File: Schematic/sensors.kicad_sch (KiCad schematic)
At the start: 17 parts, among them IC4 ICM-42688-P, IC5 MPU-6500, U5 SPL06-001, U7 QMC5883L

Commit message: schematic fully finished, every footprint assigned, still electrical checking to do
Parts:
- IC4: footprint IIM42352 -> fch7_fp:LGA-16_L3.0-W3.0-P0.50-BL_SQ
- IC5: footprint QFN40P300X300X95-25M-D -> fch7_fp:QFN40P300X300X95-25M-D
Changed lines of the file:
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@@
 			)
 		)
-		(property "Footprint" "IIM42352"
+		(property "Footprint" "fch7_fp:LGA-16_L3.0-W3.0-P0.50-BL_SQ"
 			(at 256.54 131.75 0)
 			(effects
@@
 			)
 		)
-		(property "Footprint" "QFN40P300X300X95-25M-D"
+		(property "Footprint" "fch7_fp:QFN40P300X300X95-25M-D"
 			(at 140.97 143.18 0)
 			(effects

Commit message: reviewing and refactoring footprints and full schematic
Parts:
- C28, C29, C30, C31, C32, C33, C34, C36: MPN (none) -> 0603B104K500NT; Manufacturer (none) -> FH
- C35, C37: MPN (none) -> CC0603KRX7R9BB103; Manufacturer (none) -> YAGEO
- C38: MPN (none) -> 0603B224K500NT; Manufacturer (none) -> FH
- C39: footprint Capacitor_SMD:C_0805_2012Metric -> Capacitor_SMD:C_0603_1608Metric; MPN (none) -> CL10B105KO8NNNC; Manufacturer (none) -> SAMSUNG
- IC4: MPN (none) -> ICM-42688-P; Manufacturer (none) -> TDK
- IC5: MPN (none) -> MPU-6500; Manufacturer (none) -> TDK
- R22: MPN (none) -> RC0603FR-07100KL; Manufacturer (none) -> YAGEO
- U5: MPN (none) -> SPL06-001; Manufacturer (none) -> Goertek
- U7: MPN (none) -> QMC5883L; Manufacturer (none) -> QST

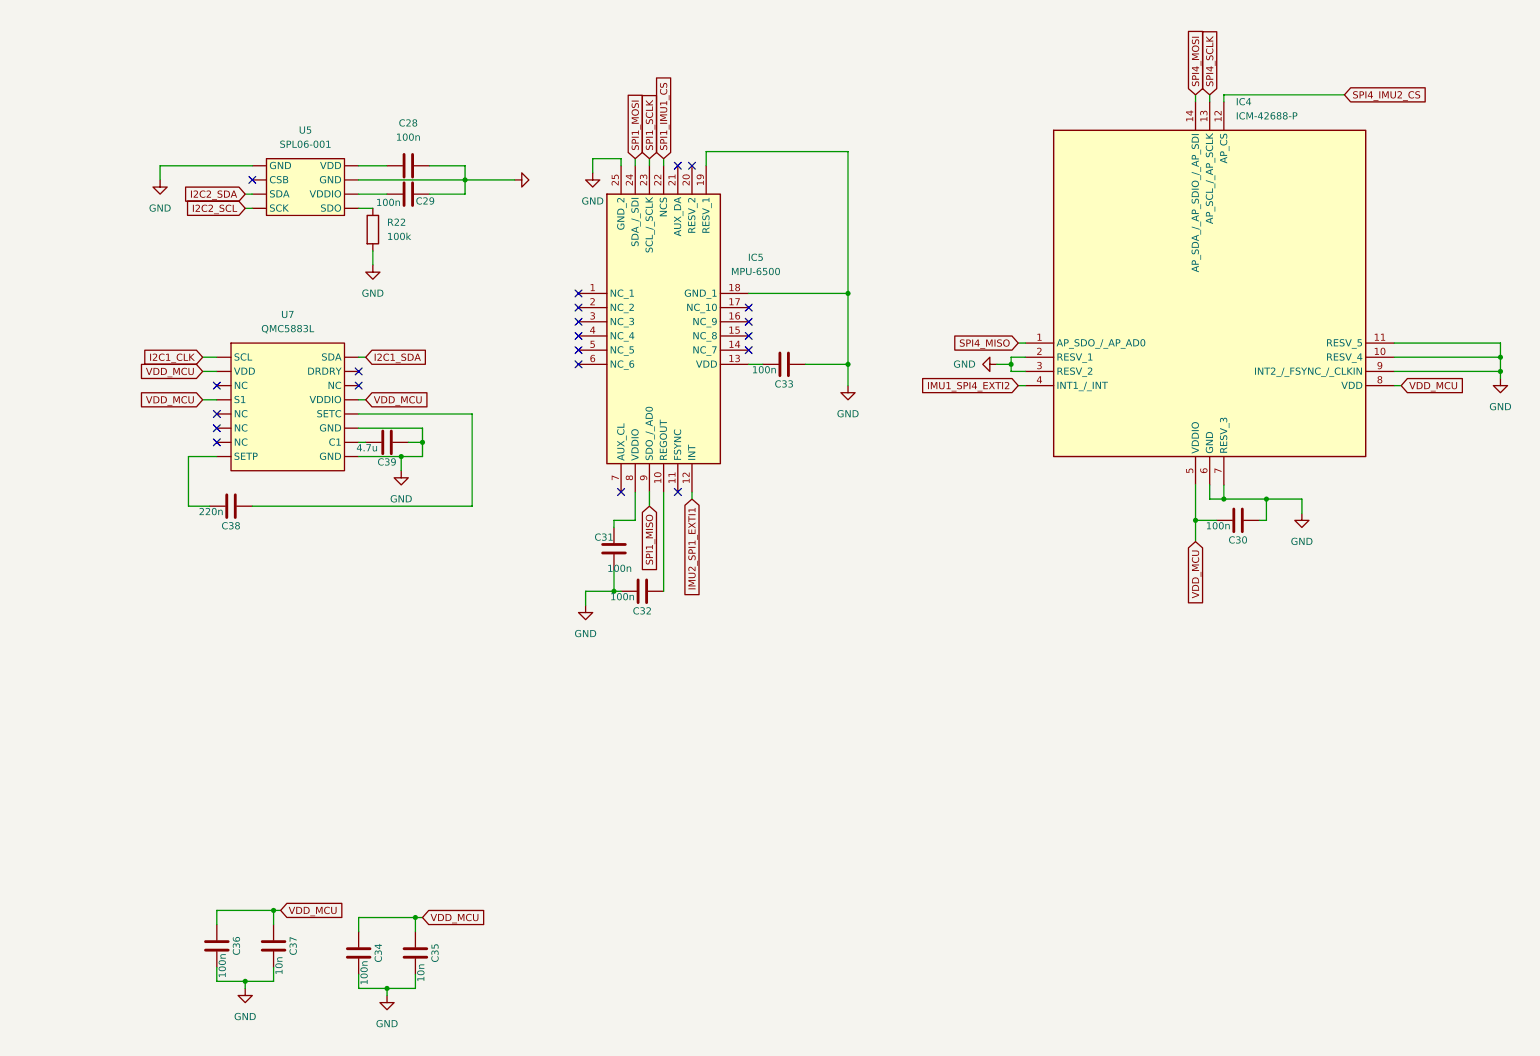
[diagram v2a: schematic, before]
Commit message: Update schematic and footprint libraries with various component modifications
- Updated fp-info-cache with new component details and footprint changes.
- Modified osd.kicad_sch to correct pin types and add no_connect entries.
- Adjusted rf_rx.kicad_sch to fix pin assignments and update component properties.
- Enhanced sensors.kicad_sch with new properties for QMC5883L and SPL06-001 sensors.
- Added new libraries to sym-lib-table and fp-lib-table for better organization and access to components.
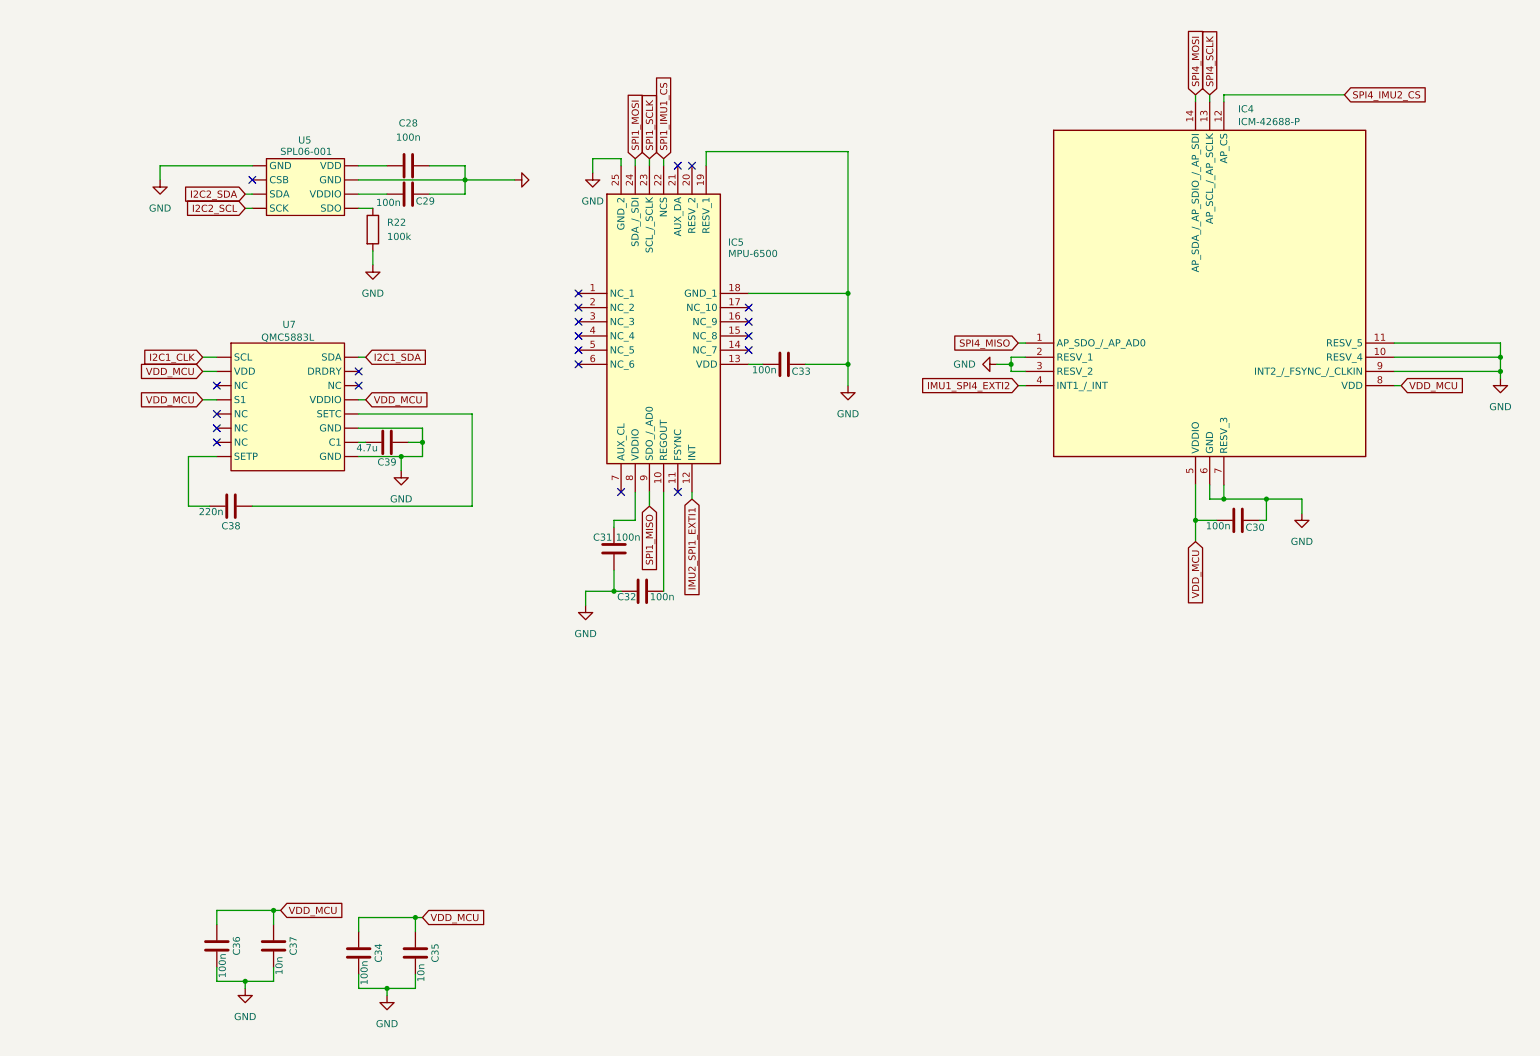
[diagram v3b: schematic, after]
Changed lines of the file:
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@@
 		(dnp no)
 		(property "Reference" "C32"
-			(at 125.73 120.396 90)
+			(at 122.936 117.856 90)
 			(effects
 				(font
@@
 		)
 		(property "Value" "100n"
-			(at 122.174 117.856 90)
+			(at 129.286 117.856 90)
 			(effects
 				(font
@@
 		(on_board yes)
 		(dnp no)
-		(fields_autoplaced yes)
 		(property "Reference" "U7"
-			(at 62.23 67.31 0)
+			(at 62.484 69.088 0)
 			(effects
 				(font
@@
 		)
 		(property "Value" "QMC5883L"
-			(at 62.23 69.85 0)
+			(at 62.23 71.374 0)
 			(effects
 				(font
@@
 		(dnp no)
 		(property "Reference" "C31"
-			(at 118.872 107.188 0)
+			(at 118.618 107.188 0)
 			(effects
 				(font
@@
 		)
 		(property "Value" "100n"
-			(at 121.666 112.776 0)
+			(at 123.19 107.188 0)
 			(effects
 				(font
@@
 		(dnp no)
 		(property "Reference" "C33"
-			(at 151.13 79.756 90)
+			(at 154.178 77.47 90)
 			(effects
 				(font
@@
 		(on_board yes)
 		(dnp no)
-		(fields_autoplaced yes)
 		(property "Reference" "IC4"
-			(at 232.0133 29.21 0)
+			(at 232.41 30.48 0)
 			(effects
 				(font
@@
 		)
 		(property "Value" "ICM-42688-P"
-			(at 232.0133 31.75 0)
+			(at 232.41 32.766 0)
 			(effects
 				(font
@@
 		(dnp no)
 		(property "Reference" "C30"
-			(at 232.41 107.696 90)
+			(at 235.458 105.41 90)
 			(effects
 				(font
@@
 		(on_board yes)
 		(dnp no)
-		(fields_autoplaced yes)
 		(property "Reference" "U5"
-			(at 65.405 34.29 0)
+			(at 65.278 36.068 0)
 			(effects
 				(font
@@
 		)
 		(property "Value" "SPL06-001"
-			(at 65.405 36.83 0)
+			(at 65.532 38.1 0)
 			(effects
 				(font
@@
 		(on_board yes)
 		(dnp no)
-		(fields_autoplaced yes)
 		(property "Reference" "IC5"
-			(at 146.05 57.0798 0)
+			(at 142.494 54.356 0)
 			(effects
 				(font
@@
 		)
 		(property "Value" "MPU-6500"
-			(at 146.05 59.6198 0)
-			(effects
-				(font
+			(at 145.542 56.388 0)
+			(effects
+				(font

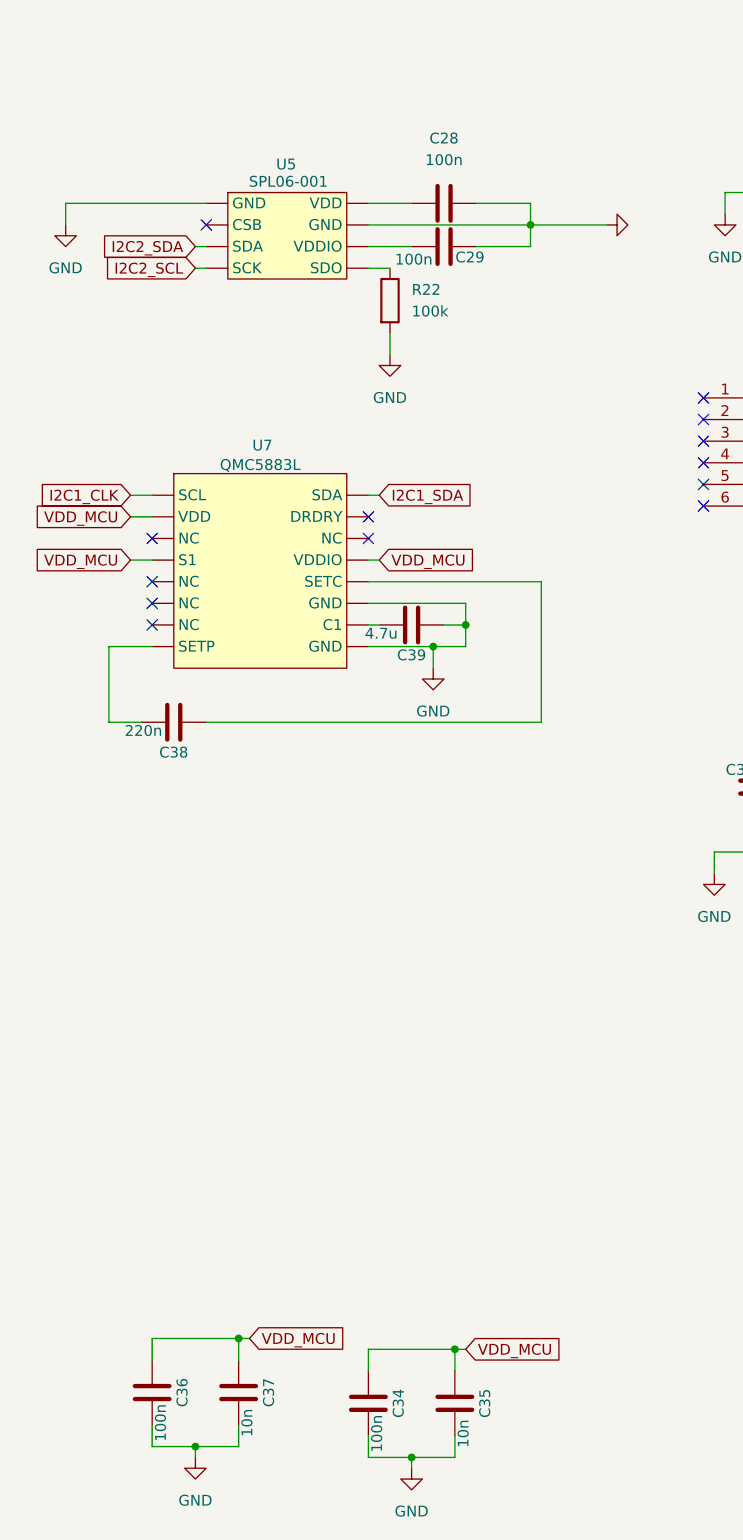
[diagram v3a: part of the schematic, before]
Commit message: Refactor fp-lib-table: Remove unused libraries and update description for fch7_fp
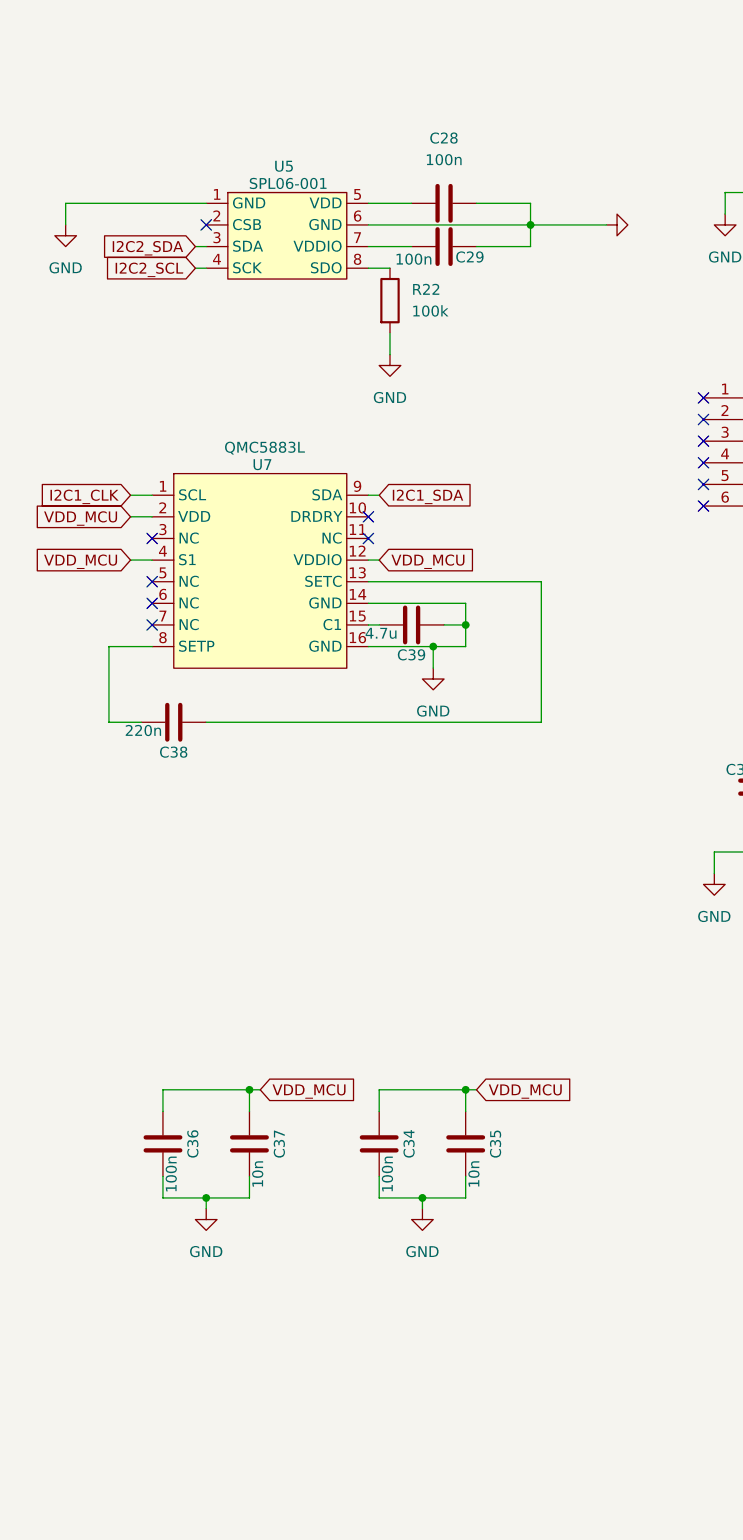
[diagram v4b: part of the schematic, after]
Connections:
- net GND: now also U5.1 (GND), U5.6 (GND), U7.14 (GND), U7.16 (GND); no longer U5. (SDO), U7. (GND)
- net I2C1_CLK: now also U7.1 (SCL); no longer U7. (GND)
- net I2C1_SDA: now also U7.9 (SDA); no longer U7. (GND)
- net I2C2_SCL: now also U5.4 (SCK); no longer U5. (SDO)
- net I2C2_SDA: now also U5.3 (SDA); no longer U5. (SDO)
- net VDD_MCU: now also U7.12 (VDDIO), U7.2 (VDD), U7.4 (S1); no longer U7. (GND)
- net at C29.1: now also U5.7 (VDDIO); no longer U5. (SDO)
- net at C38.1: now also U7.8 (SETP); no longer U7. (GND)
- net at C38.2: now also U7.13 (SETC); no longer U7. (GND)
- net at C39.1: now also U7.15 (C1); no longer U7. (GND)
- net at C28.1: now also U5.5 (VDD); no longer U5. (SDO)
- net at R22.1: now also U5.8 (SDO); no longer U5. (SDO)
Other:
- moved on the sheet: C34, C35, C36, C37
